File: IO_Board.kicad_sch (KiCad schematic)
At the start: 7 parts, among them CN301 SM32B-NSHDZS-1-TF, CN302 SM32B-NSHDZS-1-TF

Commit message: Update .gitignore, CANBus_Interface.kicad_sch, ESP32-S3_WLED_UnderGlow_Hat-2026-05-04_233126.zip, and 17 more files
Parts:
- C301: symbol Device:C_Small -> Device:C
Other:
- sheet WLED Outputs ports: added MISO; removed SDO
- moved on the sheet: C301, CN301, CN302, R301, R302

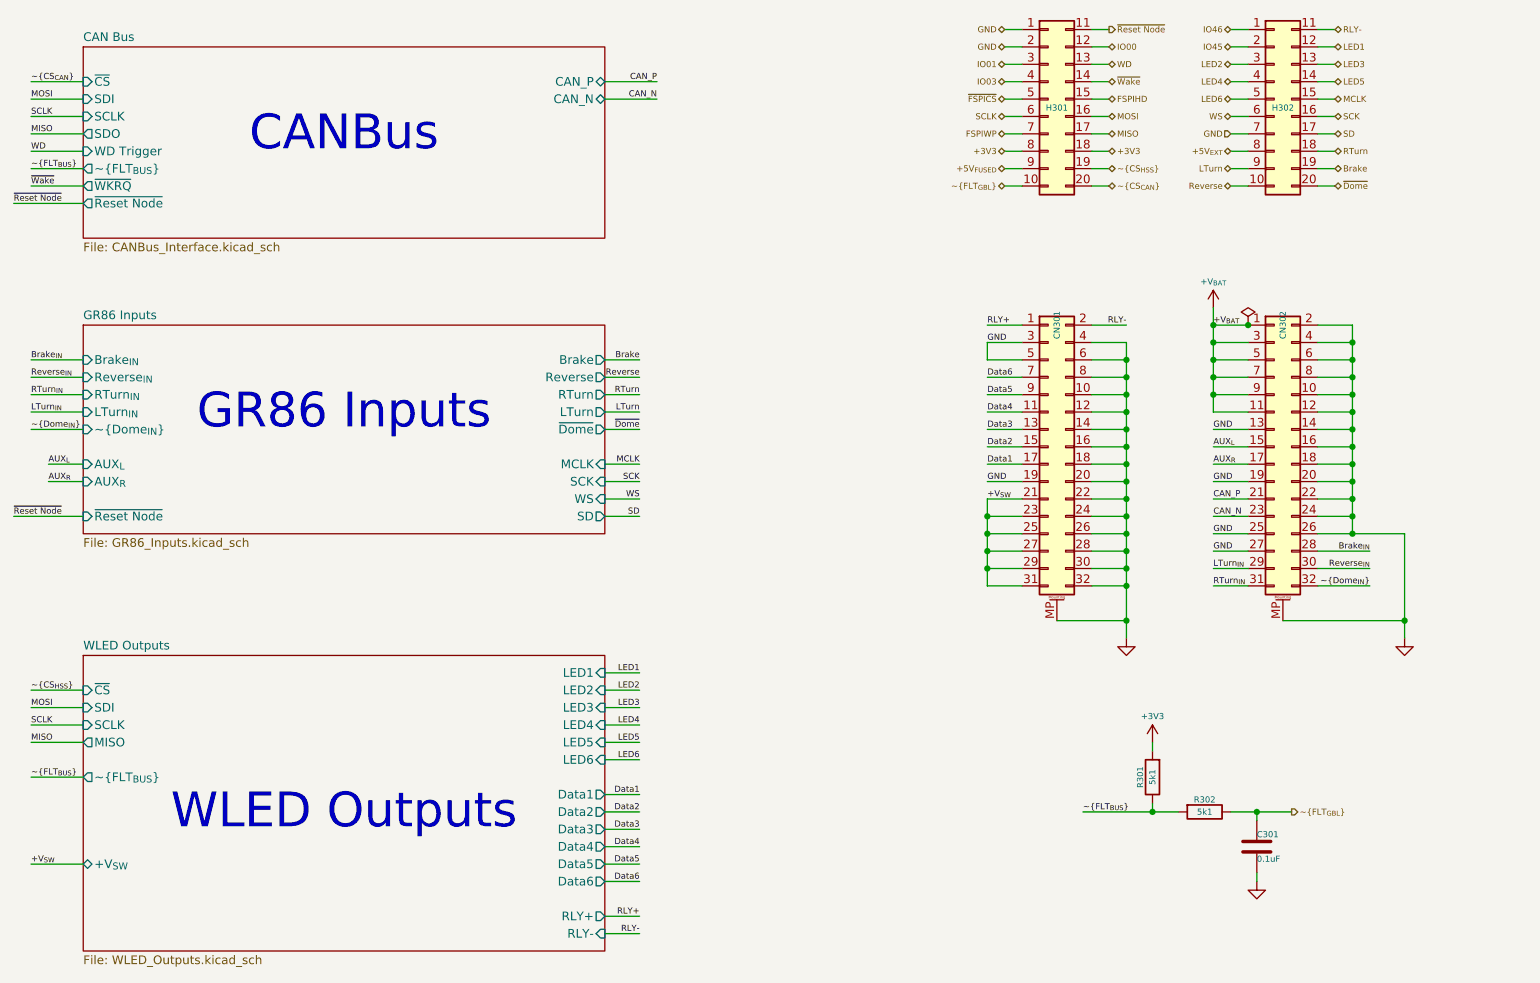
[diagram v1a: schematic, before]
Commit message: replaced Device:C with Device:C_Small and Device:R with Device:R_Small
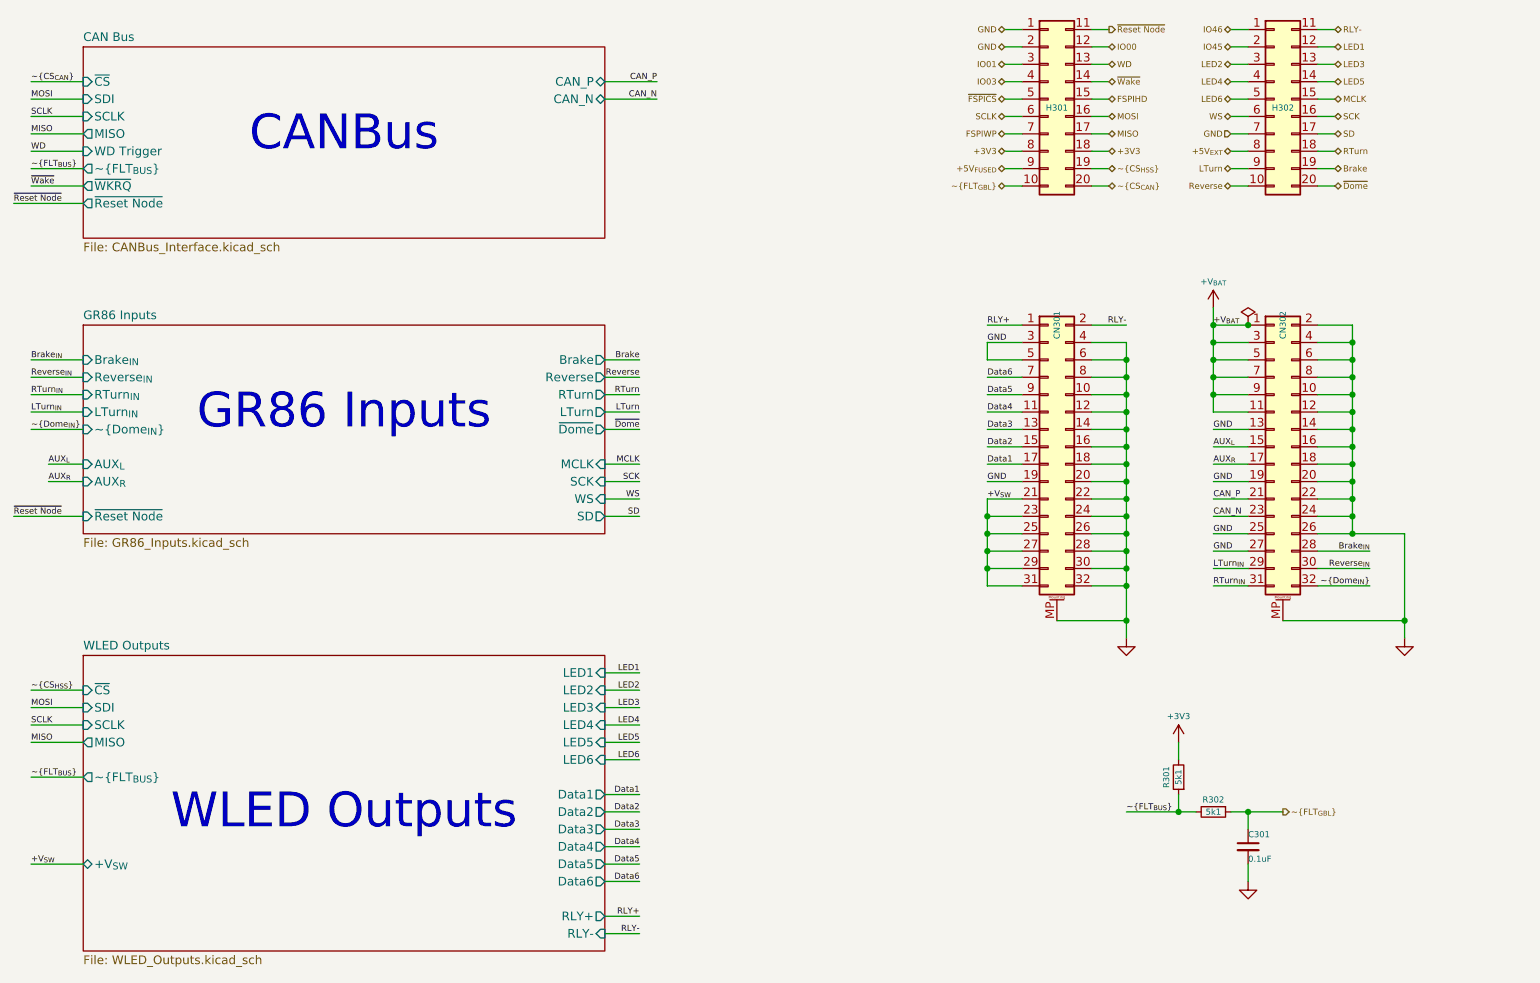
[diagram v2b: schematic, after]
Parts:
- C301: symbol Device:C -> Device:C_Small
- R301, R302: symbol Device:R -> Device:R_Small
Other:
- sheet CAN Bus ports: added MISO; removed SDO
- moved on the sheet: C301, R301, R302

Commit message: Updated Net Names for FSPI and I2S nets
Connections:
- net FSPIHD renamed FSPI_{HD}
- net FSPIWP renamed FSPI_{WP}
- net MCLK renamed I^{2}S_{MCLK}
- net MISO renamed FSPI_{MISO}
- net MOSI renamed FSPI_{MOSI}
- net SCK renamed I^{2}S_{SCK}
- net SCLK renamed FSPI_{CLK}
- net SD renamed I^{2}S_{SD}
- net WS renamed I^{2}S_{WS}
- net ~{FSPICS} renamed ~{FSPI_{CS0}}

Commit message: schematic updated with new ESP32-S3_D1_Pico symbol
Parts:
- removed H301, H302: ESP_Header, My Connectors:PinHeader_2x10_P2.54mm_Vertical_THT_BottomMount_TopReference, symbol PersonalSchematicSymbolLibrary:Conn_02x10_Top_Bottom
- added U201: ~, Personal_FootprintLibrary:ESP32-S3_D1_Pico, symbol PersonalSchematicSymbolLibrary:ESP32-S3_D1_Pico
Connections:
- net +3V3: now also U201.18 (3V3), U201.8 (3V3)
- net +5V_{EXT}: now also U201.28 (5V_{EXT})
- net +5V_{FUSED}: now also U201.9 (5V)
- net Brake: now also U201.39 (IO16)
- net FSPI_{CLK}: now also U201.6 (IO12)
- net FSPI_{HD}: now also U201.15 (IO09)
- net FSPI_{MISO}: now also U201.17 (IO13)
- net FSPI_{MOSI}: now also U201.16 (IO11)
- net FSPI_{WP}: now also U201.7 (IO14)
- net GND: now also U201.1 (GND), U201.2 (GND), U201.27 (GND)
- net IO00: now also U201.12 (IO00)
- net IO01: now also U201.3 (IO01)
- net IO03: now also U201.4 (IO03)
- net IO45: now also U201.22 (IO45)
- net IO46: now also U201.21 (IO46)
- net I^{2}S_{MCLK}: now also U201.36 (IO47)
- net I^{2}S_{SCK}: now also U201.26 (IO48)
- net I^{2}S_{SD}: now also U201.35 (IO39)
- net I^{2}S_{WS}: now also U201.37 (IO21)
- net LED1: now also U201.32 (IO44)
- net LED2: now also U201.23 (IO43)
- net LED3: now also U201.33 (IO42)
- net LED4: now also U201.24 (IO40)
- net LED5: now also U201.34 (IO41)
- net LED6: now also U201.25 (IO38)
- net LTurn: now also U201.29 (IO17)
- net RLY-: now also U201.31 (GND0)
- net RTurn: now also U201.38 (IO18)
- net Reverse: now also U201.30 (IO08)
- net WD: now also U201.13 (IO02)
- net ~{CS_{CAN}}: now also U201.20 (I005)
- net ~{CS_{HSS}}: now also U201.19 (IO06)
- net ~{Dome}: now also U201.40 (IO15)
- net ~{FLT_{GBL}}: now also U201.10 (IO07)
- net ~{FSPI_{CS0}}: now also U201.5 (IO10)
- net ~{Reset Node}: now also U201.11 (EN/~{RST})
- net ~{Wake}: now also U201.14 (IO04)
